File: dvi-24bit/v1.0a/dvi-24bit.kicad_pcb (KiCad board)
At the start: 4 copper layers, 40 x 40.8 mm, 38 parts, among them J1 PMOD, J10 sj, J2 PMOD, J3 jmp, J4 5V, J5 3v3_5v_sel, J6 HDMI_A_1.4, J7 sj, J8 sj, J9 sj, U1 VREG_3V3, U2 SII164

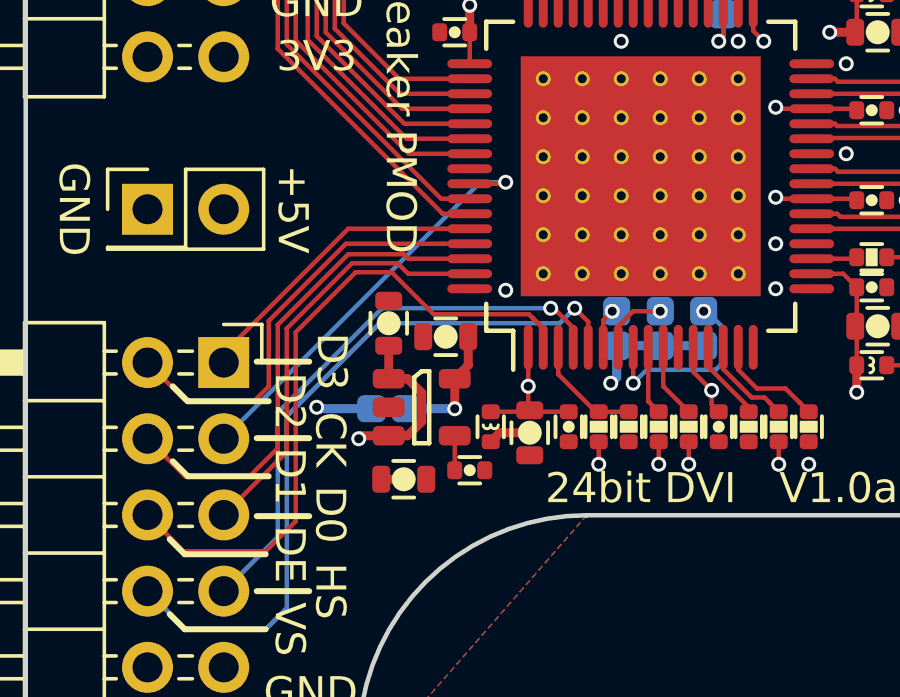
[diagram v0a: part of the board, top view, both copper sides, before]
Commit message: Moved CLK, set default DK.
* Moved CLK: This is for the iCEBreaker. It allows the use of a separate
clock and ability to rotate the clock wave by 90deg.
* As we have DKEN on by default, we should also set the jumpers to a
sane default. In this case we use the internal default of the part that
is 0b100.

Thanks for the suggestions @smunaut.
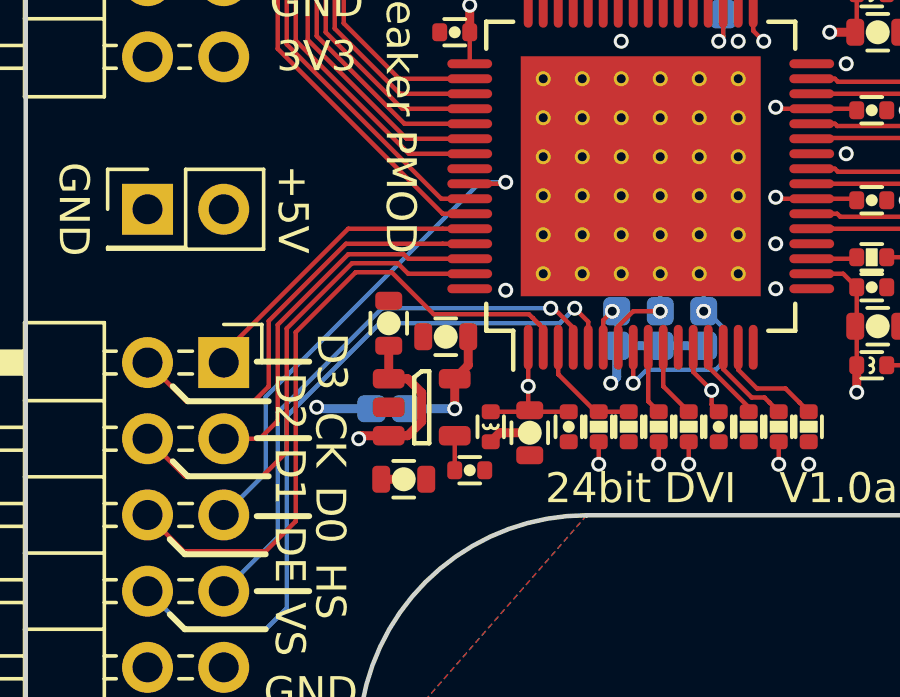
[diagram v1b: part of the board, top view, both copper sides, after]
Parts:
- J7, J8, J9: footprint pkl_jumpers:J_0903 -> pkl_jumpers:J_NCNO_0903_15
- turned J8 to 270 degrees
- turned J9 to 270 degrees
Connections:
- J1 pad 2: /CLK -> /D1
- J1 pad 3: /D0 -> /CLK
- J1 pad 8: /D1 -> /D0
- J8 pad 1: +3V3 -> GND
- J8 pad 3: GND -> +3V3
- J9 pad 1: +3V3 -> GND
- J9 pad 3: GND -> +3V3
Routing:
- net /D1: track 16.8 -> 12.7 mm
- net /D0: track 14.2 -> 16.8 mm
- net /CLK: track 14.2 -> 16.7 mm

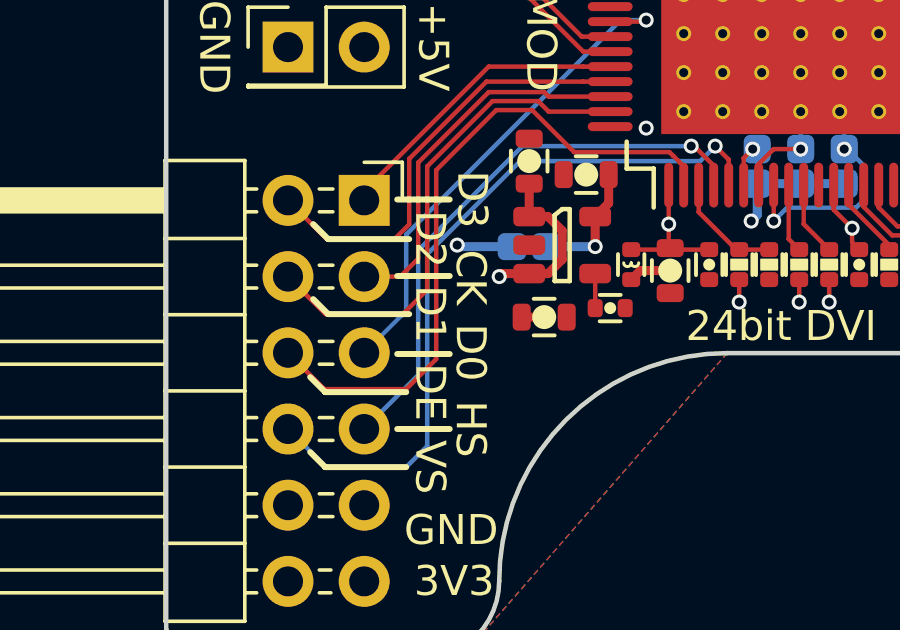
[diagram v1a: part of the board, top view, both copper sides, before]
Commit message: Corrected silkscreen legend.
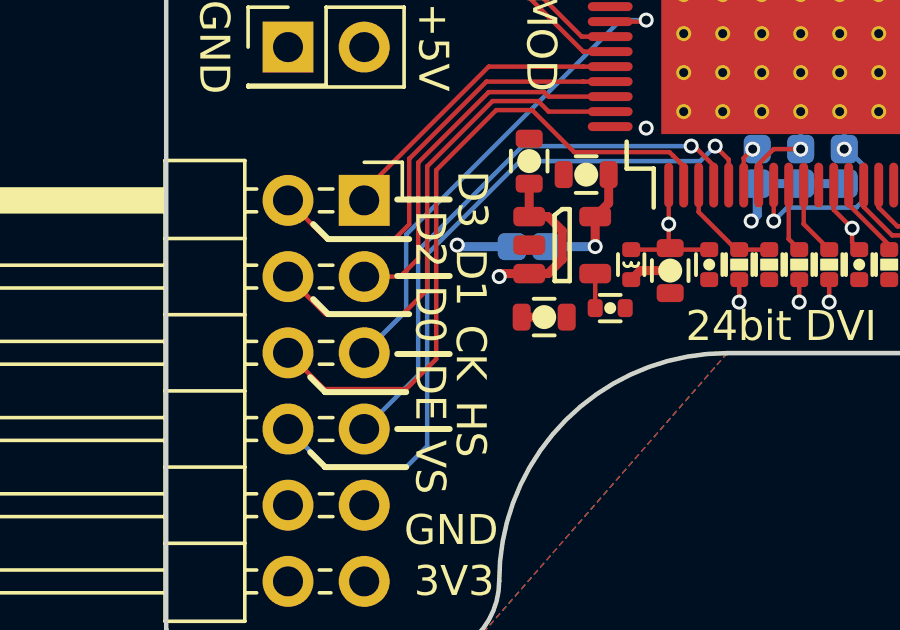
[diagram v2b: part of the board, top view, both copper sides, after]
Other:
- board text added: "CLK"
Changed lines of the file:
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@@
     (effects (font (size 1 1) (thickness 0.25)) (justify mirror))
   )
-  (gr_text D1 (at 32.2 47.85) (layer B.SilkS)
+  (gr_text D0 (at 32.2 47.85) (layer B.SilkS)
     (effects (font (size 1 1) (thickness 0.25)) (justify mirror))
   )
-  (gr_text CK (at 38.45 47.88) (layer B.SilkS)
+  (gr_text D1 (at 38.45 47.88) (layer B.SilkS)
     (effects (font (size 1 1) (thickness 0.25)) (justify mirror))
   )
@@
     (effects (font (size 1 1) (thickness 0.25)) (justify mirror))
   )
-  (gr_text D0 (at 38.5 50.4) (layer B.SilkS)
+  (gr_text CLK (at 38.5 50.4) (layer B.SilkS)
     (effects (font (size 1 1) (thickness 0.25)) (justify mirror))
   )
@@
     (effects (font (size 1 1) (thickness 0.25)))
   )
-  (gr_text D0 (at 40.15 50.38 270) (layer F.SilkS)
+  (gr_text CK (at 40.15 50.38 270) (layer F.SilkS)
     (effects (font (size 1 1) (thickness 0.25)))
   )
@@
     (effects (font (size 1 1) (thickness 0.25)))
   )
-  (gr_text CK (at 40.15 47.88 270) (layer F.SilkS)
+  (gr_text D1 (at 40.15 47.88 270) (layer F.SilkS)
     (effects (font (size 1 1) (thickness 0.25)))
   )
-  (gr_text D1 (at 38.8 49.1 270) (layer F.SilkS)
+  (gr_text D0 (at 38.8 49.1 270) (layer F.SilkS)
     (effects (font (size 1 1) (thickness 0.25)))
   )

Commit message: Minor fixes.
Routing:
- net GND: vias 22 -> 25
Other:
- rule pad_to_mask_clearance: 0.05 -> 0.01
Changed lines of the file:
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@@
     (thickness 1.6)
     (drawings 104)
-    (tracks 355)
+    (tracks 358)
     (zones 0)
     (modules 38)
@@
     (pad_size 1.7 1.7)
     (pad_drill 1)
-    (pad_to_mask_clearance 0.05)
+    (pad_to_mask_clearance 0.01)
     (solder_mask_min_width 0.25)
     (aux_axis_origin 70 60.6)
@@
   (gr_line (start 70 31) (end 70 49.4) (layer Edge.Cuts) (width 0.15))
   (gr_line (start 48.7 30) (end 69 30) (layer Edge.Cuts) (width 0.15))
-  (via (at 49.85 34.6) (size 0.5) (drill 0.3) (layers F.Cu B.Cu) (net 1))
+  (via (at 46 34.7) (size 0.5) (drill 0.3) (layers F.Cu B.Cu) (net 1))
   (via (at 53.75 34.6) (size 0.5) (drill 0.3) (layers F.Cu B.Cu) (net 1))
   (via (at 60.2 37.45) (size 0.5) (drill 0.3) (layers F.Cu B.Cu) (net 1))
@@
   (segment (start 52.25 33.4) (end 52.25 32.3) (width 0.15) (layer F.Cu) (net 1))
   (segment (start 52.75 33.4) (end 52.75 32.3) (width 0.15) (layer F.Cu) (net 1))
+  (via (at 46 40.2) (size 0.5) (drill 0.3) (layers F.Cu B.Cu) (net 1))
+  (via (at 43.5 42.9) (size 0.5) (drill 0.3) (layers F.Cu B.Cu) (net 1))
+  (via (at 52.4 34.6) (size 0.5) (drill 0.3) (layers F.Cu B.Cu) (net 1))
   (segment (start 45.5 47.95) (end 45.8 47.65) (width 0.3) (layer F.Cu) (net 2))
   (via (at 46.8 47.65) (size 0.5) (drill 0.3) (layers F.Cu B.Cu) (net 2))
@@
   (segment (start 53.25 34.45) (end 53.25 33.4) (width 0.15) (layer F.Cu) (net 23))
   (segment (start 53.1 34.6) (end 53.25 34.45) (width 0.15) (layer F.Cu) (net 23))
-  (via (at 46 39.3) (size 0.5) (drill 0.3) (layers F.Cu B.Cu) (net 24))
-  (segment (start 45.95 39.35) (end 46 39.3) (width 0.15) (layer F.Cu) (net 24))
-  (segment (start 44.8 39.35) (end 45.95 39.35) (width 0.15) (layer F.Cu) (net 24))
-  (segment (start 38 46.45) (end 45.15 39.3) (width 0.15) (layer B.Cu) (net 24))
   (segment (start 36.6 50.39) (end 38 48.99) (width 0.15) (layer B.Cu) (net 24))
-  (segment (start 45.15 39.3) (end 46 39.3) (width 0.15) (layer B.Cu) (net 24))
-  (segment (start 38 48.99) (end 38 46.45) (width 0.15) (layer B.Cu) (net 24))
+  (segment (start 45.85 39.35) (end 46 39.5) (width 0.15) (layer F.Cu) (net 24))
+  (via (at 46 39.5) (size 0.5) (drill 0.3) (layers F.Cu B.Cu) (net 24))
+  (segment (start 38 46.946447) (end 45.446447 39.5) (width 0.15) (layer B.Cu) (net 24))
+  (segment (start 45.646447 39.5) (end 46 39.5) (width 0.15) (layer B.Cu) (net 24))
+  (segment (start 44.8 39.35) (end 45.85 39.35) (width 0.15) (layer F.Cu) (net 24))
+  (segment (start 45.446447 39.5) (end 45.646447 39.5) (width 0.15) (layer B.Cu) (net 24))
+  (segment (start 38 48.99) (end 38 46.946447) (width 0.15) (layer B.Cu) (net 24))
   (segment (start 41.525 46.85) (end 39.75 46.85) (width 0.3) (layer B.Cu) (net 50))
   (via (at 39.7 46.8) (size 0.5) (drill 0.3) (layers F.Cu B.Cu) (net 50))
@@
   (segment (start 54.25 34.25) (end 54.6 34.6) (width 0.15) (layer F.Cu) (net 27))
   (segment (start 54.25 33.4) (end 54.25 34.25) (width 0.15) (layer F.Cu) (net 27))
-  (segment (start 54 35.2) (end 54.6 34.6) (width 0.3) (layer In1.Cu) (net 27))
-  (segment (start 46.550001 35.649999) (end 47 35.2) (width 0.3) (layer In1.Cu) (net 27))
-  (segment (start 47 35.2) (end 54 35.2) (width 0.3) (layer In1.Cu) (net 27))
-  (segment (start 46.550001 45.950001) (end 46.550001 35.649999) (width 0.3) (layer In1.Cu) (net 27))
-  (segment (start 46.75 46.1) (end 46.7 46.1) (width 0.3) (layer In1.Cu) (net 27))
-  (segment (start 46.7 46.1) (end 46.550001 45.950001) (width 0.3) (layer In1.Cu) (net 27))
   (segment (start 53.1 46.95) (end 52.864105 46.714105) (width 0.15) (layer F.Cu) (net 27))
   (segment (start 47.25 46.6) (end 52.5 46.6) (width 0.3) (layer In1.Cu) (net 27))
@@
   (via (at 52.864105 46.235895) (size 0.5) (drill 0.3) (layers F.Cu B.Cu) (net 27))
   (segment (start 52.5 46.6) (end 52.864105 46.235895) (width 0.3) (layer In1.Cu) (net 27))
+  (segment (start 54.350001 34.849999) (end 54.6 34.6) (width 0.3) (layer In1.Cu) (net 27))
+  (segment (start 47 35.2) (end 54 35.2) (width 0.3) (layer In1.Cu) (net 27))
+  (segment (start 46.75 46.1) (end 46.550001 45.900001) (width 0.3) (layer In1.Cu) (net 27))
+  (segment (start 46.550001 35.649999) (end 47 35.2) (width 0.3) (layer In1.Cu) (net 27))
+  (segment (start 46.550001 45.900001) (end 46.550001 35.649999) (width 0.3) (layer In1.Cu) (net 27))
+  (segment (start 54 35.2) (end 54.350001 34.849999) (width 0.3) (layer In1.Cu) (net 27))
   (segment (start 57.7 44.15) (end 57.65 44.1) (width 0.15) (layer F.Cu) (net 28))
   (segment (start 57.7 45.4) (end 57.7 44.15) (width 0.15) (layer F.Cu) (net 28))
@@
   (via (at 44.8 33.4) (size 0.5) (drill 0.3) (layers F.Cu B.Cu) (net 28))
   (segment (start 44.8 33.4) (end 44.8 34.3) (width 0.3) (layer F.Cu) (net 28))
-  (segment (start 45.4 34) (end 44.8 33.4) (width 0.3) (layer In1.Cu) (net 28))
-  (segment (start 45.4 45.564002) (end 45.4 34) (width 0.3) (layer In1.Cu) (net 28))
-  (segment (start 46.886007 47.050009) (end 45.4 45.564002) (width 0.3) (layer In1.Cu) (net 28))
-  (segment (start 51.9364 47.05001) (end 46.886007 47.050009) (width 0.3) (layer In1.Cu) (net 28))
-  (segment (start 57.7 46.3) (end 56.949991 47.050009) (width 0.3) (layer In1.Cu) (net 28))
-  (segment (start 56.949991 47.050009) (end 51.9364 47.05001) (width 0.3) (layer In1.Cu) (net 28))
+  (segment (start 44.8 33.753553) (end 44.8 33.4) (width 0.3) (layer In1.Cu) (net 28))
+  (segment (start 44.8 44.964002) (end 44.8 33.753553) (width 0.3) (layer In1.Cu) (net 28))
+  (segment (start 46.886007 47.050009) (end 44.8 44.964002) (width 0.3) (layer In1.Cu) (net 28))
+  (segment (start 57.7 46.3) (end 56.94999 47.05001) (width 0.3) (layer In1.Cu) (net 28))
+  (segment (start 56.94999 47.05001) (end 46.886007 47.050009) (width 0.3) (layer In1.Cu) (net 28))
   (segment (start 49.25 43.9) (end 49.25 44.8) (width 0.15) (layer F.Cu) (net 29))
   (via (at 49.55 43.6) (size 0.5) (drill 0.3) (layers F.Cu B.Cu) (net 29))

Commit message: Adjusted solderstop webbing min width.
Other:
- rule solder_mask_min_width: 0.25 -> 0.05
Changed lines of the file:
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@@
     (pad_drill 1)
     (pad_to_mask_clearance 0.01)
-    (solder_mask_min_width 0.25)
+    (solder_mask_min_width 0.05)
     (aux_axis_origin 70 60.6)
     (grid_origin 30 40.2)

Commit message: Some global cleanup.
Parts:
- added REF**: null_Logo_SilkS_7.5mm, pkl_logos:null_Logo_SilkS_7.5mm, B.Cu at (48.1, 37.1)
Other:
- board text added: "NULL"
- board text removed: "1BitSquared"
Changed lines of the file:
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@@
-(kicad_pcb (version 20171130) (host pcbnew 5.1.5-52549c5~84~ubuntu19.10.1)
+(kicad_pcb (version 20171130) (host pcbnew 5.1.5-52549c5~86~ubuntu19.10.1)
   (general
     (thickness 1.6)
@@
     (tracks 358)
     (zones 0)
-    (modules 38)
+    (modules 39)
     (nets 51)
   )
@@
     (add_net "Net-(J6-Pad19)")
     (add_net "Net-(U2-Pad11)")
+  )
+  (module pkl_logos:null_Logo_SilkS_7.5mm (layer B.Cu)
+    (at 48.1 37.1 90)
+    (fp_text reference REF** (at 0 -5 90) (layer B.Fab)
+      (effects (font (size 1 1) (thickness 0.15)) (justify mirror))
+    )
+    (fp_text value null_Logo_SilkS_7.5mm (at 0 5 90) (layer B.Fab)
+      (effects (font (size 1 1) (thickness 0.15)) (justify mirror))
+    )
+    (fp_line (start 1 -0.5) (end 1.5 -0.5) (layer B.SilkS) (width 0.15))
+    (fp_line (start 1 0.5) (end 1 -0.5) (layer B.SilkS) (width 0.15))
+    (fp_line (start 0.2 -0.5) (end 0.7 -0.5) (layer B.SilkS) (width 0.15))
+    (fp_line (start 0.2 0.5) (end 0.2 -0.5) (layer B.SilkS) (width 0.15))
+    (fp_line (start -0.1 -0.2) (end -0.1 0.5) (layer B.SilkS) (width 0.15))
+    (fp_arc (start -0.4 -0.2) (end -0.7 -0.2) (angle 180) (layer B.SilkS) (width 0.15))
+    (fp_line (start -0.7 0.5) (end -0.7 -0.2) (layer B.SilkS) (width 0.15))
+    (fp_line (start -1 -0.5) (end -1 0.5) (layer B.SilkS) (width 0.15))
+    (fp_line (start -1.5 0.5) (end -1 -0.5) (layer B.SilkS) (width 0.15))
+    (fp_line (start -1.5 -0.5) (end -1.5 0.5) (layer B.SilkS) (width 0.15))
+    (fp_line (start 3.75 3.75) (end -3.75 3.75) (layer B.SilkS) (width 0.3))
+    (fp_line (start -3.75 3.75) (end -3.75 -3.75) (layer B.SilkS) (width 0.3))
+    (fp_line (start 3.75 3.75) (end 3.75 -3.75) (layer B.SilkS) (width 0.3))
+    (fp_line (start -3.75 -3.75) (end 3.75 -3.75) (layer B.SilkS) (width 0.3))
   )
   (module pkl_jumpers:J_NCNO_0903_15 (layer B.Cu)
@@
     (effects (font (size 1 1) (thickness 0.2)) (justify mirror))
   )
-  (gr_text 1BitSquared (at 42.3 37.15 270) (layer B.SilkS)
+  (gr_text NULL (at 42.3 37.15 270) (layer B.SilkS)
     (effects (font (size 1.5 1.5) (thickness 0.3)) (justify mirror))
   )
@@
   (via (at 59.85 34.3) (size 0.5) (drill 0.3) (layers F.Cu B.Cu) (net 1))
   (via (at 59.4 38.35) (size 0.5) (drill 0.3) (layers F.Cu B.Cu) (net 1))
-  (via (at 44.3 46.85) (size 0.5) (drill 0.3) (layers F.Cu B.Cu) (net 2))
-  (segment (start 42.675 46.85) (end 44.3 46.85) (width 0.3) (layer B.Cu) (net 2))
-  (segment (start 44.3 46.85) (end 44.3 45.849999) (width 0.3) (layer F.Cu) (net 2))
-  (segment (start 44.75 45.399999) (end 44.3 45.849999) (width 0.3) (layer F.Cu) (net 2))
-  (segment (start 44.75 44.45) (end 44.75 45.399999) (width 0.3) (layer F.Cu) (net 2))
-  (via (at 42.6 49.2) (size 0.5) (drill 0.3) (layers F.Cu B.Cu) (net 2))
-  (segment (start 41.85 49.2) (end 42.6 49.2) (width 0.3) (layer F.Cu) (net 2))
-  (via (at 49.1 48.7) (size 0.5) (drill 0.3) (layers F.Cu B.Cu) (net 2))
-  (segment (start 49.1 47.95) (end 49.1 48.7) (width 0.15) (layer F.Cu) (net 2))
-  (via (at 51.1 48.7) (size 0.5) (drill 0.3) (layers F.Cu B.Cu) (net 2))
-  (segment (start 51.1 47.95) (end 51.1 48.7) (width 0.15) (layer F.Cu) (net 2))
-  (via (at 52.1 48.7) (size 0.5) (drill 0.3) (layers F.Cu B.Cu) (net 2))
-  (segment (start 52.1 47.95) (end 52.1 48.7) (width 0.15) (layer F.Cu) (net 2))
   (via (at 56.1 48.7) (size 0.5) (drill 0.3) (layers F.Cu B.Cu) (net 1))
   (via (at 46 42.9) (size 0.5) (drill 0.3) (layers F.Cu B.Cu) (net 1))
@@
   (via (at 43.5 42.9) (size 0.5) (drill 0.3) (layers F.Cu B.Cu) (net 1))
   (via (at 52.4 34.6) (size 0.5) (drill 0.3) (layers F.Cu B.Cu) (net 1))
+  (via (at 44.3 46.85) (size 0.5) (drill 0.3) (layers F.Cu B.Cu) (net 2))
+  (segment (start 42.675 46.85) (end 44.3 46.85) (width 0.3) (layer B.Cu) (net 2))
+  (segment (start 44.3 46.85) (end 44.3 45.849999) (width 0.3) (layer F.Cu) (net 2))
+  (segment (start 44.75 45.399999) (end 44.3 45.849999) (width 0.3) (layer F.Cu) (net 2))
+  (segment (start 44.75 44.45) (end 44.75 45.399999) (width 0.3) (layer F.Cu) (net 2))
+  (via (at 42.6 49.2) (size 0.5) (drill 0.3) (layers F.Cu B.Cu) (net 2))
+  (segment (start 41.85 49.2) (end 42.6 49.2) (width 0.3) (layer F.Cu) (net 2))
+  (via (at 49.1 48.7) (size 0.5) (drill 0.3) (layers F.Cu B.Cu) (net 2))
+  (segment (start 49.1 47.95) (end 49.1 48.7) (width 0.15) (layer F.Cu) (net 2))
+  (via (at 51.1 48.7) (size 0.5) (drill 0.3) (layers F.Cu B.Cu) (net 2))
+  (segment (start 51.1 47.95) (end 51.1 48.7) (width 0.15) (layer F.Cu) (net 2))
+  (via (at 52.1 48.7) (size 0.5) (drill 0.3) (layers F.Cu B.Cu) (net 2))
+  (segment (start 52.1 47.95) (end 52.1 48.7) (width 0.15) (layer F.Cu) (net 2))
   (segment (start 45.5 47.95) (end 45.8 47.65) (width 0.3) (layer F.Cu) (net 2))
   (via (at 46.8 47.65) (size 0.5) (drill 0.3) (layers F.Cu B.Cu) (net 2))
@@
   (segment (start 45.446447 39.5) (end 45.646447 39.5) (width 0.15) (layer B.Cu) (net 24))
   (segment (start 38 48.99) (end 38 46.946447) (width 0.15) (layer B.Cu) (net 24))
-  (segment (start 41.525 46.85) (end 39.75 46.85) (width 0.3) (layer B.Cu) (net 50))
-  (via (at 39.7 46.8) (size 0.5) (drill 0.3) (layers F.Cu B.Cu) (net 50))
-  (segment (start 39.75 46.85) (end 39.7 46.8) (width 0.3) (layer B.Cu) (net 50))
   (segment (start 57.65 41.85) (end 57.7 41.8) (width 0.15) (layer F.Cu) (net 25))
   (segment (start 56.2 41.85) (end 57.65 41.85) (width 0.15) (layer F.Cu) (net 25))
@@
   (segment (start 37.89 49.1) (end 38.69999 48.29001) (width 0.15) (layer F.Cu) (net 48))
   (segment (start 35.31 49.1) (end 37.89 49.1) (width 0.15) (layer F.Cu) (net 48))
+  (segment (start 41.525 46.85) (end 39.75 46.85) (width 0.3) (layer B.Cu) (net 50))
+  (via (at 39.7 46.8) (size 0.5) (drill 0.3) (layers F.Cu B.Cu) (net 50))
+  (segment (start 39.75 46.85) (end 39.7 46.8) (width 0.3) (layer B.Cu) (net 50))
   (zone (net 1) (net_name GND) (layer F.Cu) (hatch edge 0.508)
     (connect_pads (clearance 0.15))
